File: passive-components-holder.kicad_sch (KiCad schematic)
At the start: 99 parts

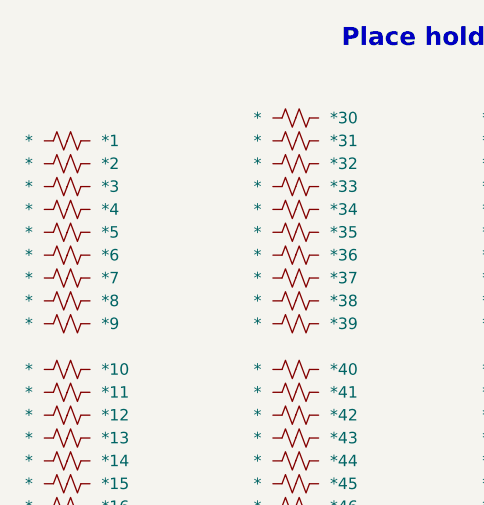
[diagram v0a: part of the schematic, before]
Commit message: Placement and main labels in place
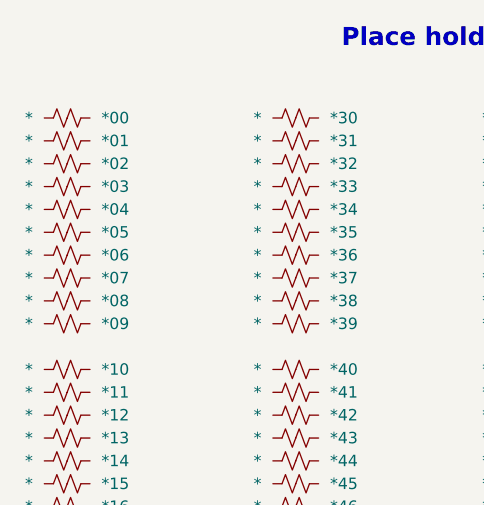
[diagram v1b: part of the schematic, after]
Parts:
- added *00: *, component_holder:component_holder_THT_pitches_200_300_400_500_mils, symbol Device:R_Small_US
- *01: renamed from *1; footprint (none) -> component_holder:component_holder_THT_pitches_200_300_400_500_mils
- *02: renamed from *2; footprint (none) -> component_holder:component_holder_THT_pitches_200_300_400_500_mils
- *03: renamed from *3; footprint (none) -> component_holder:component_holder_THT_pitches_200_300_400_500_mils
- *04: renamed from *4; footprint (none) -> component_holder:component_holder_THT_pitches_200_300_400_500_mils
- *05: renamed from *5; footprint (none) -> component_holder:component_holder_THT_pitches_200_300_400_500_mils
- *06: renamed from *6; footprint (none) -> component_holder:component_holder_THT_pitches_200_300_400_500_mils
- *07: renamed from *7; footprint (none) -> component_holder:component_holder_THT_pitches_200_300_400_500_mils
- *08: renamed from *8; footprint (none) -> component_holder:component_holder_THT_pitches_200_300_400_500_mils
- *09: renamed from *9; footprint (none) -> component_holder:component_holder_THT_pitches_200_300_400_500_mils
- *10, *11, *12, *13, *14, *15, *16, *17, *18, *19, *20, *21, *22, *23, *24, *25, *26, *27, *28, *29, *30, *31, *32, *33, *34, *35, *36, *37, *38, *39, *40, *41, *42, *43, *44, *45, *46, *47, *48, *49, *50, *51, *52, *53, *54, *55, *56, *57, *58, *59, *60, *61, *62, *63, *64, *65, *66, *67, *68, *69, *70, *71, *72, *73, *74, *75, *76, *77, *78, *79, *80, *81, *82, *83, *84, *85, *86, *87, *88, *89, *90, *91, *92, *93, *94, *95, *96, *97, *98, *99: footprint (none) -> component_holder:component_holder_THT_pitches_200_300_400_500_mils

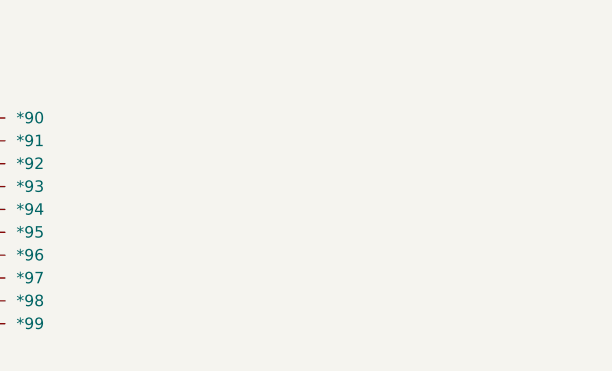
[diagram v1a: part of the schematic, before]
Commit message: finished v1 : mounting holes, outline shape, tweak orientation description
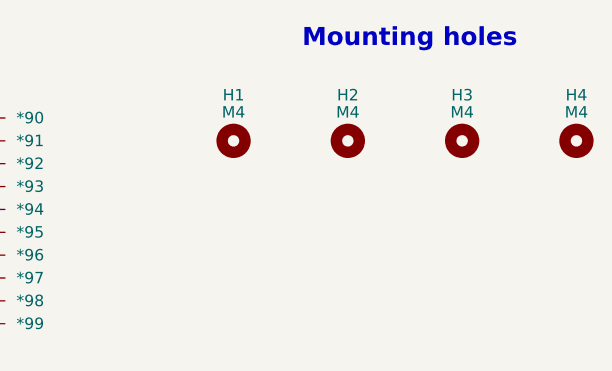
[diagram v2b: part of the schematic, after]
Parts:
- added H1, H2, H3, H4: M4, MountingHole:MountingHole_4.3mm_M4, symbol Mechanical:MountingHole
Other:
- note added: "Mounting holes"
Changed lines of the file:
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@@
   (title_block
     (title "Passive components holder")
-    (date "2024-05-04")
-    (rev "DRAFT")
+    (date "2024-05-05")
+    (rev "v1.0.0")
     (company "Sporniket")
     (comment 3 "https://github.com/sporniket/passive-components-holder")
     (comment 4 "Original repository : ")
   )
+  (text "Mounting holes" (at 147.32 27.94 0)
+    (effects (font (size 2 2) (thickness 0.4) bold) (justify left bottom))
+  )
   (text "Place holders" (at 66.04 27.94 0)
     (effects (font (size 2 2) (thickness 0.4) bold) (justify left bottom))
@@
     )
   )
+  (symbol (lib_id "Mechanical:MountingHole") (at 177.8 38.1 0) (unit 1)
+    (in_bom yes) (on_board yes) (dnp no)
+    (property "Reference" "H4" (at 177.8 33.02 0)
+      (effects (font (size 1.27 1.27)))
+    )
+    (property "Value" "M4" (at 177.8 34.925 0)
+      (effects (font (size 1.27 1.27)))
+    )
+    (property "Footprint" "MountingHole:MountingHole_4.3mm_M4" (at 177.8 38.1 0)
+      (effects (font (size 1.27 1.27)) hide)
+    )
+    (property "Datasheet" "~" (at 177.8 38.1 0)
+      (effects (font (size 1.27 1.27)) hide)
+    )
+    (instances
+      (project "passive-components-holder"
+        (path "/b1733103-db4d-43f2-8c35-85b1a36f2c38"
+          (reference "H4") (unit 1)
+        )
+      )
+    )
+  )
   (symbol (lib_id "Device:R_Small_US") (at 86.36 99.06 90) (unit 1)
     (in_bom yes) (on_board yes) (dnp no)
@@
     )
   )
+  (symbol (lib_id "Mechanical:MountingHole") (at 152.4 38.1 0) (unit 1)
+    (in_bom yes) (on_board yes) (dnp no)
+    (property "Reference" "H2" (at 152.4 33.02 0)
+      (effects (font (size 1.27 1.27)))
+    )
+    (property "Value" "M4" (at 152.4 34.925 0)
+      (effects (font (size 1.27 1.27)))
+    )
+    (property "Footprint" "MountingHole:MountingHole_4.3mm_M4" (at 152.4 38.1 0)
+      (effects (font (size 1.27 1.27)) hide)
+    )
+    (property "Datasheet" "~" (at 152.4 38.1 0)
+      (effects (font (size 1.27 1.27)) hide)
+    )
+    (instances
+      (project "passive-components-holder"
+        (path "/b1733103-db4d-43f2-8c35-85b1a36f2c38"
+          (reference "H2") (unit 1)
+        )
+      )
+    )
+  )
   (symbol (lib_id "Device:R_Small_US") (at 35.56 73.66 90) (unit 1)
     (in_bom yes) (on_board yes) (dnp no)
@@
     )
   )
+  (symbol (lib_id "Mechanical:MountingHole") (at 139.7 38.1 0) (unit 1)
+    (in_bom yes) (on_board yes) (dnp no)
+    (property "Reference" "H1" (at 139.7 33.02 0)
+      (effects (font (size 1.27 1.27)))
+    )
+    (property "Value" "M4" (at 139.7 34.925 0)
+      (effects (font (size 1.27 1.27)))
+    )
+    (property "Footprint" "MountingHole:MountingHole_4.3mm_M4" (at 139.7 38.1 0)
+      (effects (font (size 1.27 1.27)) hide)
+    )
+    (property "Datasheet" "~" (at 139.7 38.1 0)
+      (effects (font (size 1.27 1.27)) hide)
+    )
+    (instances
+      (project "passive-components-holder"
+        (path "/b1733103-db4d-43f2-8c35-85b1a36f2c38"
+          (reference "H1") (unit 1)
+        )
+      )
+    )
+  )
   (symbol (lib_id "Device:R_Small_US") (at 86.36 53.34 90) (unit 1)
     (in_bom yes) (on_board yes) (dnp no)
@@
         )
       )
+    )
+  )
+  (symbol (lib_id "Mechanical:MountingHole") (at 165.1 38.1 0) (unit 1)
+    (in_bom yes) (on_board yes) (dnp no)
+    (property "Reference" "H3" (at 165.1 33.02 0)
+      (effects (font (size 1.27 1.27)))
+    )
+    (property "Value" "M4" (at 165.1 34.925 0)
+      (effects (font (size 1.27 1.27)))
+    )
+    (property "Footprint" "MountingHole:MountingHole_4.3mm_M4" (at 165.1 38.1 0)
+      (effects (font (size 1.27 1.27)) hide)
+    )
+    (property "Datasheet" "~" (at 165.1 38.1 0)
+      (effects (font (size 1.27 1.27)) hide)
+    )
+    (instances
+      (project "passive-components-holder"
+        (path "/b1733103-db4d-43f2-8c35-85b1a36f2c38"
+          (reference "H3") (unit 1)
+        )
+      )
